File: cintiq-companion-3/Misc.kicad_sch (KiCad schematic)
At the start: 2 parts, among them U1 BIOS_1, U2 BIOS_2

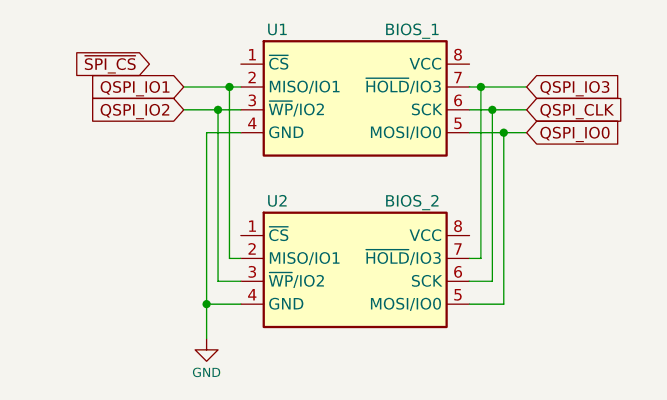
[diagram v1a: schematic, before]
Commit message: Started adding type-c
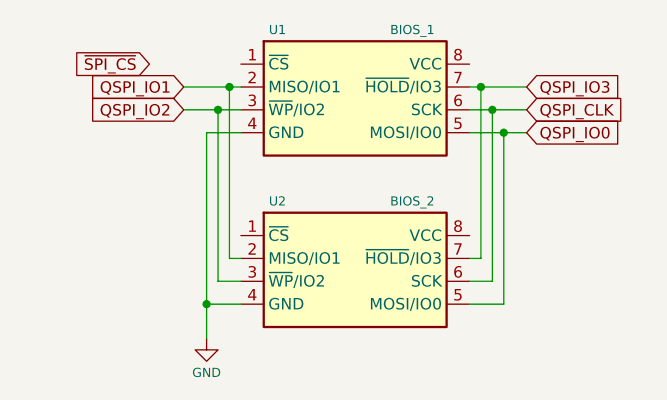
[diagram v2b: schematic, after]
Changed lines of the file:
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@@
 			(effects
 				(font
-					(size 1.27 1.27)
+					(size 1.016 1.016)
 				)
 			)
@@
 			(effects
 				(font
-					(size 1.27 1.27)
+					(size 1.016 1.016)
 				)
 			)
@@
 			(effects
 				(font
-					(size 1.27 1.27)
+					(size 1.016 1.016)
 				)
 			)
@@
 			(effects
 				(font
-					(size 1.27 1.27)
+					(size 1.016 1.016)
 				)
 			)
